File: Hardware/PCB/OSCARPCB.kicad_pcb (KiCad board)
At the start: 2 copper layers, 1 part

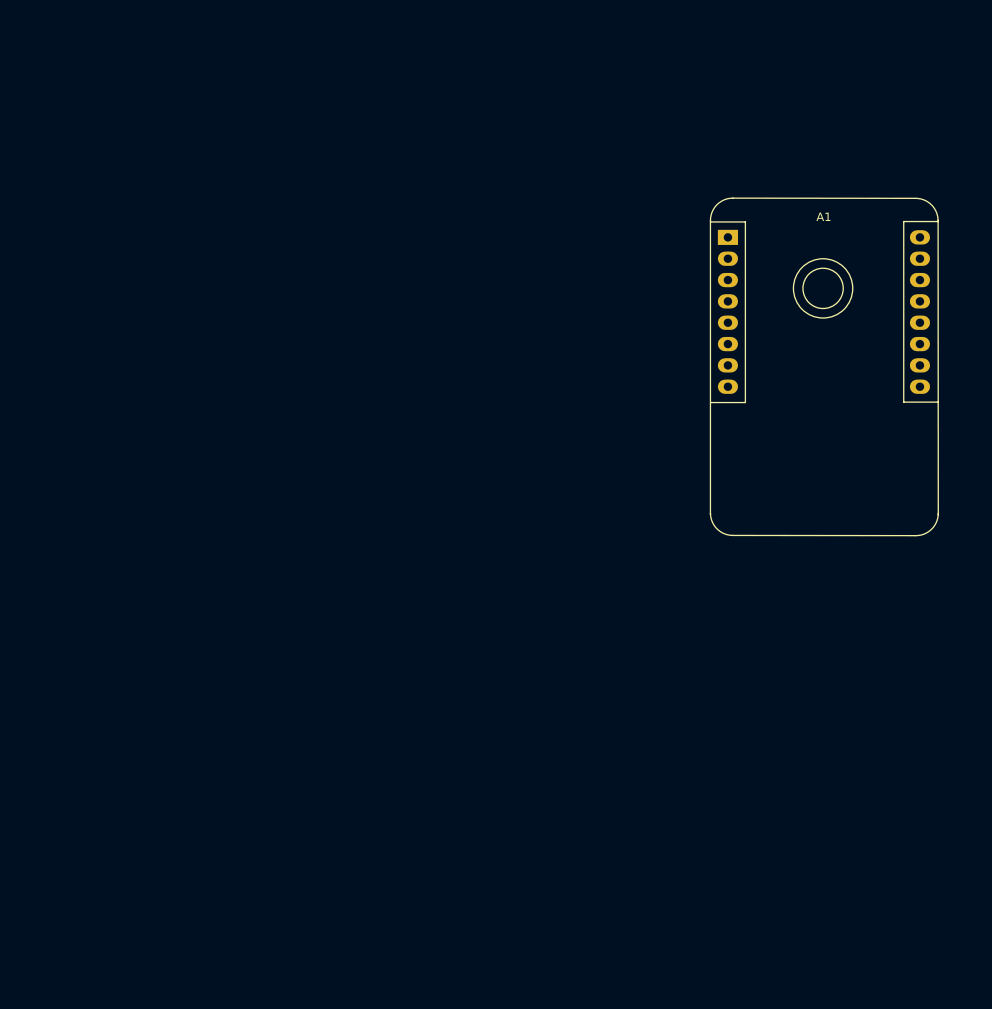
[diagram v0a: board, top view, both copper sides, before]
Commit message: Started routing PCB
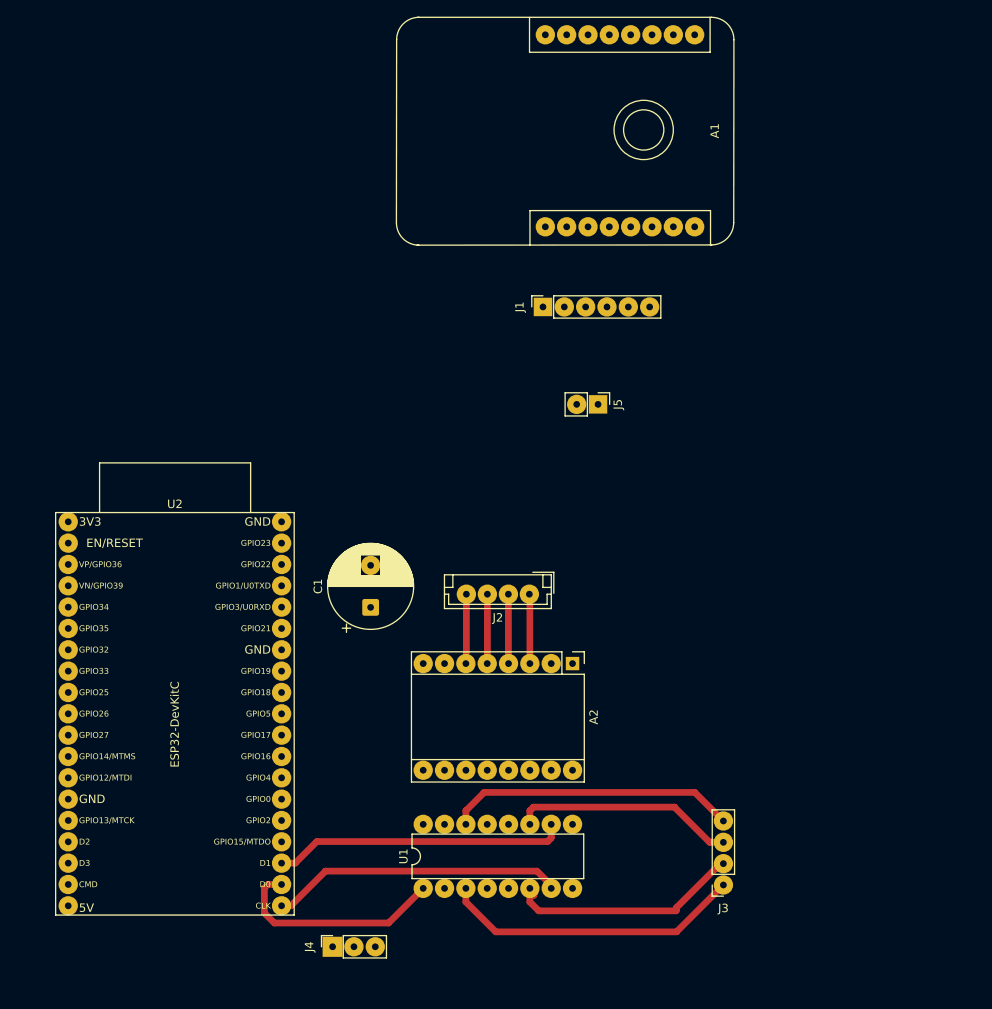
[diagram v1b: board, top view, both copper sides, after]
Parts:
- added A2: Pololu_Breakout_DRV8825, Module:Pololu_Breakout-16_15.2x20.3mm, F.Cu at (95.6, 106.5)
- added C1: 220uF_50V, Capacitor_THT:CP_Radial_D10.0mm_P5.00mm, F.Cu at (71.6, 99.8)
- added J1: CP2102 IN, Connector_PinSocket_2.54mm:PinSocket_1x06_P2.54mm_Vertical, F.Cu at (92.1, 64.0)
- added J2: Stepper Motor OUT, Connector_JST:JST_EH_B4B-EH-A_1x04_P2.50mm_Vertical, F.Cu at (90.5, 98.2)
- added J3: DC Motors OUT, Connector_PinSocket_2.54mm:PinSocket_1x04_P2.54mm_Vertical, F.Cu at (113.6, 132.8)
- added J4: Servo OUT, Connector_PinSocket_2.54mm:PinSocket_1x03_P2.54mm_Vertical, F.Cu at (67.1, 140.2)
- added J5: Power Input, Connector_PinHeader_2.54mm:PinHeader_1x02_P2.54mm_Vertical, F.Cu at (98.7, 75.6)
- added U1: L293D, Package_DIP:DIP-16_W7.62mm, F.Cu at (77.9, 133.2)
- added U2: ESP32-DevKitC, PCM_Espressif:ESP32-DevKitC, F.Cu at (35.6, 89.6)
- moved A1 36.7 mm to (98.3, 42.9), turned to -90 degrees
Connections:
- A1 pad 10: unconnected-(A1-TX-Pad10) -> Net-(A1-TX)
- A1 pad 11: unconnected-(A1-RX-Pad11) -> Net-(A1-RX)
- A1 pad 12: unconnected-(A1-VCC-Pad12) -> VBATT
- A1 pad 13: unconnected-(A1-GND-Pad13) -> GND
- A1 pad 2: unconnected-(A1-GND-Pad2) -> GND
- A1 pad 9: unconnected-(A1-GND-Pad9) -> GND
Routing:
- net /L Motor +: track 0.00 -> 36.1 mm
- net /R Motor 3: track 0.00 -> 35.0 mm
- net /L Motor 2: track 0.00 -> 34.9 mm
- net /R Motor -: track 0.00 -> 34.6 mm
- net /L Motor -: track 0.00 -> 30.5 mm
- net /R Motor +: track 0.00 -> 26.6 mm
- net /L Motor EN: track 0.00 -> 26.3 mm
- net /S. B2: track 0.00 -> 8.28 mm
- net /S. A2: track 0.00 -> 8.28 mm
- net /S. B1: track 0.00 -> 8.27 mm
- net /S. A1: track 0.00 -> 8.27 mm

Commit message: changed sch to fit PCB better
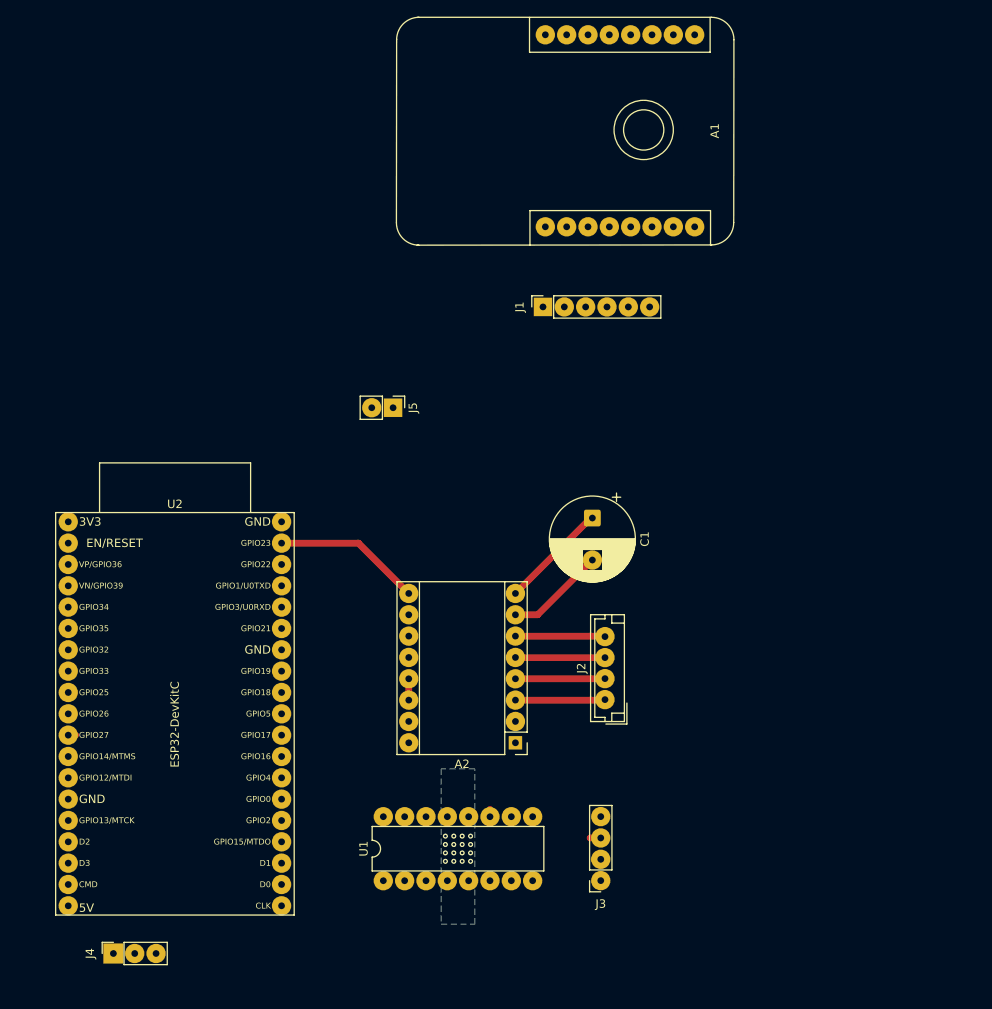
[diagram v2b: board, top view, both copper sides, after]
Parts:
- moved C1 28.5 mm to (98.0, 89.1), turned to -90 degrees
- moved J4 26.1 mm to (41.0, 141.0)
- moved J5 24.4 mm to (74.3, 76.0)
- moved J2 15.4 mm to (99.5, 110.8), turned to 90 degrees
- moved J3 14.6 mm to (99.0, 132.3)
- moved A2 11.6 mm to (88.8, 115.9), turned to 180 degrees
- moved U1 4.84 mm to (73.1, 132.3)
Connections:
- A2 pad 10: /S. M0 -> unconnected-(A2-M0-Pad10)
- A2 pad 9: /S. EN -> EN
- U2 pad 37: /S. M0 -> EN
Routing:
- net /L Motor +: track 36.1 -> 0.00 mm
- net /R Motor 3: track 35.0 -> 0.00 mm
- net /L Motor 2: track 34.9 -> 0.00 mm
- net /R Motor -: track 34.6 -> 0.00 mm
- net /L Motor -: track 30.5 -> 0.81 mm
- net /L Motor EN: track 26.3 -> 0.63 mm
- net /R Motor +: track 26.6 -> 2.16 mm
- net EN: track 0.00 -> 17.6 mm
- net VMOT: track 0.00 -> 12.9 mm
- net GND: track 0.00 -> 11.9 mm, vias 0 -> 16
- net /S. SLP + RST: track 0.00 -> 2.54 mm
- net /S. B1: track 8.27 -> 10.7 mm
- net /S. A2: track 8.28 -> 10.7 mm
- net /S. A1: track 8.27 -> 10.7 mm
- net /S. B2: track 8.28 -> 10.7 mm
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- added copper zone on B.Cu, net GND

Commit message: PCB V1
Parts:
- removed A1: ESP32_CAM, PCM_SL_Development_Boards:ESP32-CAM
- removed J1: CP2102 IN, Connector_PinSocket_2.54mm:PinSocket_1x06_P2.54mm_Vertical
- added CAM Power: PINHD_1x2_Female, Connector_PinSocket_2.54mm:PinSocket_1x02_P2.54mm_Vertical, F.Cu at (72.5, 78.5)
- DC Motors: renamed from J3
- Power In: renamed from J5
- Stepper Motor: renamed from J2
- moved Servo 23.4 mm to (64.4, 141.0)
- moved Power In 9.87 mm to (70.2, 85.0), turned to 90 degrees
- renumbered J4 to Servo
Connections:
- net /L Motor 2 renamed Net-(U1-2A)
- net /S. SLP + RST renamed SLP / RST
- A2 pad 10: unconnected-(A2-M0-Pad10) -> M0
- A2 pad 11: /S. M1 -> M1
- A2 pad 12: /S. M2 -> M2
- A2 pad 15: /S. STEP -> STEP
- A2 pad 16: /S. DIR -> DIR
- A2 pad 2: /S. FLT -> FLT
- A2 pad 7: GND -> GND VMOT
- C1 pad 2: GND -> GND VMOT
- Servo pad 1: /Servo PWM -> Net-(U2-MTCK/GPIO13/ADC2_CH4)
- U1 pad 1: /L Motor EN -> Net-(U1-EN1,2)
- U1 pad 10: /R Motor 3 -> R Motor 3
- U1 pad 15: /R Motor 4 -> R Motor 4
- U1 pad 2: /L Motor 1 -> Net-(U1-1A)
- U1 pad 9: /R Motor EN -> R EN
- U2 pad 10: /S. M2 -> unconnected-(U2-DAC_2/ADC2_CH9/GPIO26-Pad10)
- U2 pad 11: /L Motor 1 -> unconnected-(U2-ADC2_CH7/GPIO27-Pad11)
- U2 pad 15: unconnected-(U2-MTCK/GPIO13/ADC2_CH4-Pad15) -> Net-(U2-MTCK/GPIO13/ADC2_CH4)
- U2 pad 16: NC -> unconnected-(U2-SD_DATA2/GPIO9-Pad16)
- U2 pad 17: NC -> unconnected-(U2-SD_DATA3/GPIO10-Pad17)
- U2 pad 18: NC -> unconnected-(U2-CMD-Pad18)
- U2 pad 21: /L Motor EN -> Net-(U1-1A)
- U2 pad 22: /R Motor 3 -> Net-(U1-EN1,2)
- U2 pad 23: /Servo PWM -> unconnected-(U2-MTDO/GPIO15/ADC2_CH3-Pad23)
- U2 pad 24: unconnected-(U2-ADC2_CH2/GPIO2-Pad24) -> R Motor 4
- U2 pad 26: unconnected-(U2-ADC2_CH0/GPIO4-Pad26) -> R Motor 3
- U2 pad 27: /R Motor 4 -> R EN
- U2 pad 28: /R Motor EN -> DIR
- U2 pad 29: /S. FLT -> STEP
- U2 pad 31: /S. EN -> M2
- U2 pad 33: /S. STEP -> M1
- U2 pad 36: /S. DIR -> M0
- U2 pad 9: /S. M1 -> unconnected-(U2-DAC_1/ADC2_CH8/GPIO25-Pad9)
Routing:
- net GND: track 11.9 -> 175.7 mm, vias 16 -> 0
- net VBATT: track 0.00 -> 136.8 mm
- net Net-(U2-MTCK/GPIO13/ADC2_CH4): track 0.00 -> 35.4 mm
- net R EN: track 0.00 -> 33.8 mm
- net R Motor 3: track 0.00 -> 30.2 mm
- net /L Motor +: track 0.00 -> 29.8 mm
- net Net-(U1-2A): track 0.00 -> 29.8 mm
- net /R Motor -: track 0.00 -> 29.5 mm
- net SLP / RST: track 2.54 -> 20.4 mm
- net M0: track 0.00 -> 17.6 mm
- net Net-(U1-1A): track 0.00 -> 17.1 mm
- net R Motor 4: track 0.00 -> 16.9 mm
- net M2: track 0.00 -> 15.8 mm
- net STEP: track 0.00 -> 15.5 mm
- net DIR: track 0.00 -> 15.5 mm
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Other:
- board outline added: 77.5 x 73 mm

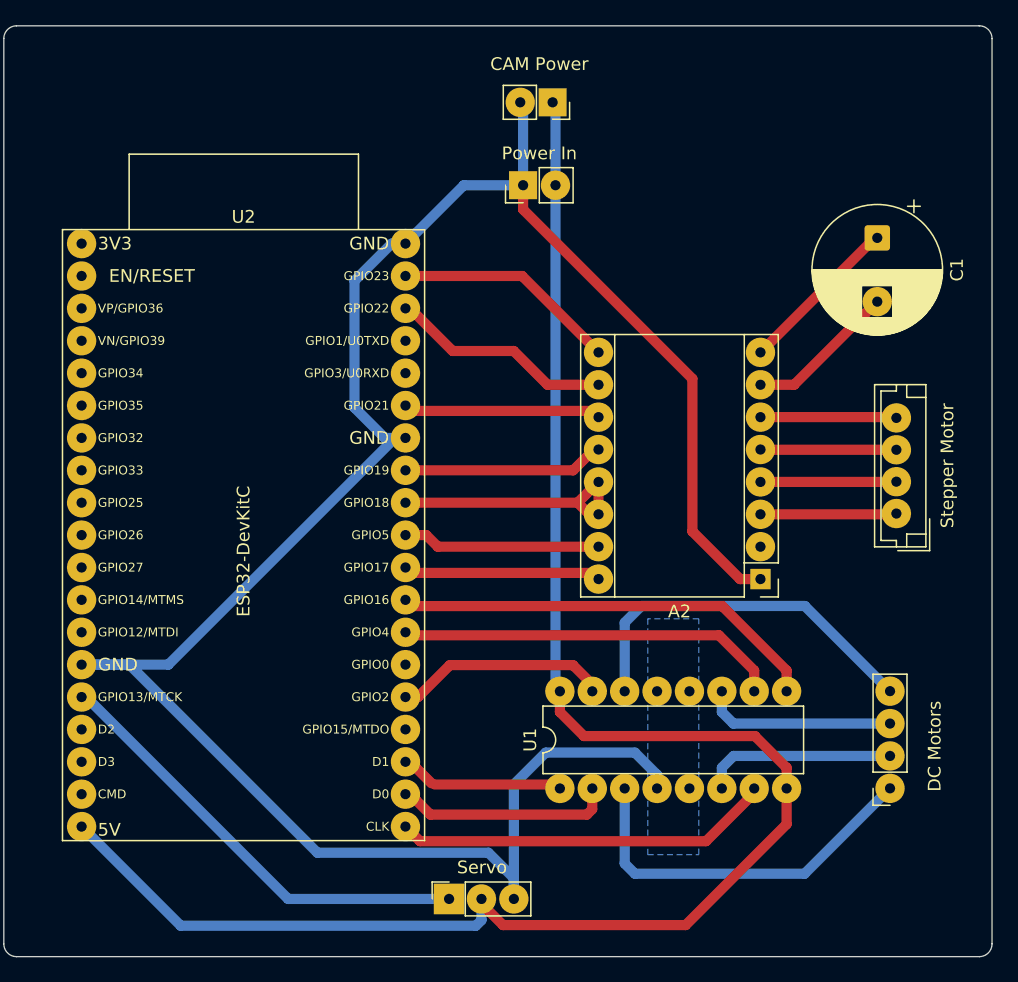
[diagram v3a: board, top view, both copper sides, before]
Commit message: Updated PCB becasue Im using external components
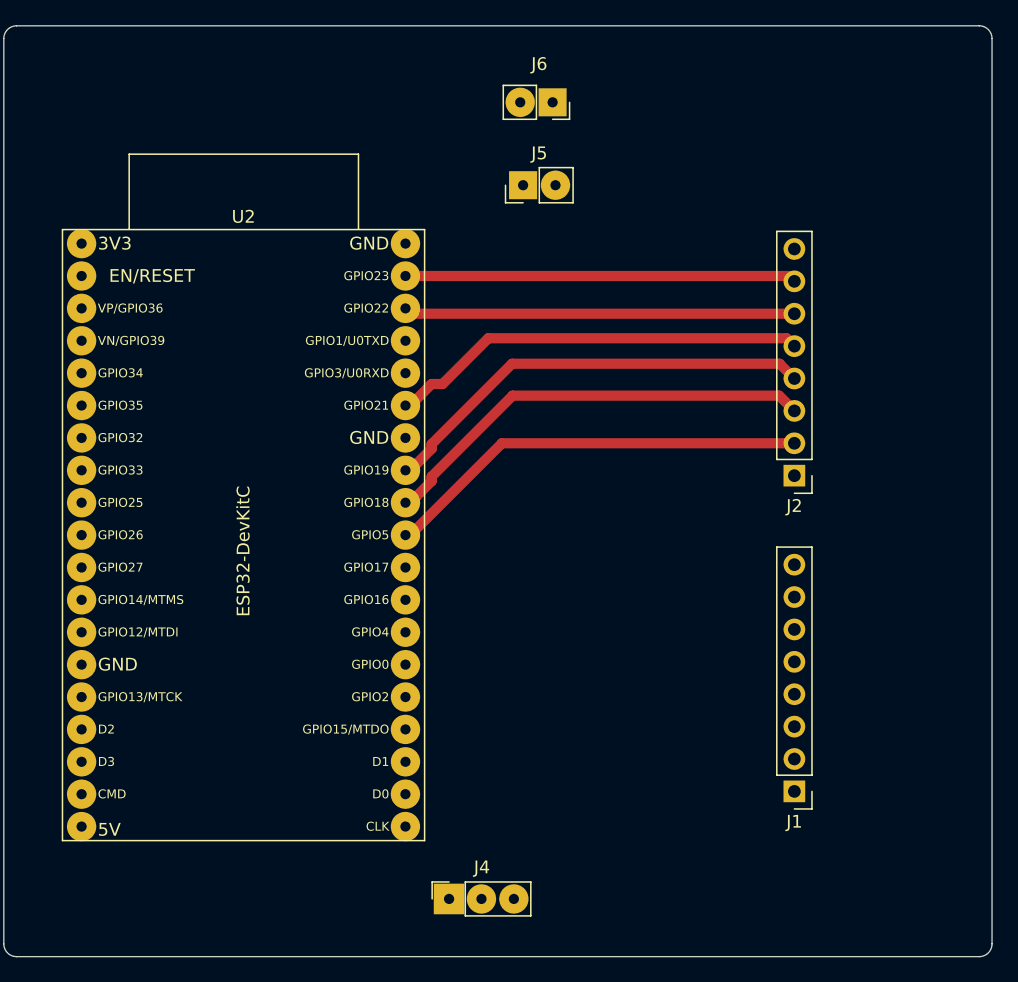
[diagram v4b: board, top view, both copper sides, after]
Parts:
- removed A2: Pololu_Breakout_DRV8825, Module:Pololu_Breakout-16_15.2x20.3mm
- removed C1: 220uF_50V, Capacitor_THT:CP_Radial_D10.0mm_P5.00mm
- removed DC Motors: DC Motors OUT, Connector_PinSocket_2.54mm:PinSocket_1x04_P2.54mm_Vertical
- removed Stepper Motor: Stepper Motor OUT, Connector_JST:JST_EH_B4B-EH-A_1x04_P2.50mm_Vertical
- removed U1: L293D, Package_DIP:DIP-16_W7.62mm
- added J1: PINHD_1x8_Male, Connector_PinHeader_2.54mm:PinHeader_1x08_P2.54mm_Vertical, F.Cu at (91.5, 132.5)
- added J2: PINHD_1x8_Male, Connector_PinHeader_2.54mm:PinHeader_1x08_P2.54mm_Vertical, F.Cu at (91.5, 107.8)
- J5: renamed from Power In
- J6: renamed from CAM Power
- renumbered Servo to J4
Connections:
- U2 pad 29: STEP -> Net-(U2-GPIO5)
- U2 pad 30: SLP / RST -> Net-(U2-GPIO18)
- U2 pad 31: M2 -> Net-(U2-GPIO19)
- U2 pad 33: M1 -> Net-(U2-GPIO21)
- U2 pad 36: M0 -> Net-(U2-GPIO22)
- U2 pad 37: EN -> Net-(U2-GPIO23)
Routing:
- net GND: track 175.7 -> 0.00 mm
- net VBATT: track 136.8 -> 0.00 mm
- net Net-(U2-MTCK/GPIO13/ADC2_CH4): track 35.4 -> 0.00 mm
- net Net-(U2-GPIO18): track 0.00 -> 34.7 mm
- net Net-(U2-GPIO19): track 0.00 -> 34.7 mm
- net R EN: track 33.8 -> 0.00 mm
- net Net-(U2-GPIO5): track 0.00 -> 33.5 mm
- net Net-(U2-GPIO21): track 0.00 -> 32.9 mm
- net Net-(U2-GPIO23): track 0.00 -> 30.7 mm
- net Net-(U2-GPIO22): track 0.00 -> 30.7 mm
- net R Motor 3: track 30.2 -> 0.00 mm
- net /L Motor +: track 29.8 -> 0.00 mm
- net Net-(U2-SD_CLK/GPIO6): track 29.8 -> 0.00 mm
- net /R Motor -: track 29.5 -> 0.00 mm
- net SLP / RST: track 20.4 -> 0.00 mm
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- removed copper zone on B.Cu, net GND

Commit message: PCB Done?
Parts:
- J1: value PINHD_1x8_Male -> DC Motor; footprint Connector_PinHeader_2.54mm:PinHeader_1x08_P2.54mm_Vertical -> Connector_PinHeader_2.54mm:PinHeader_1x06_P2.54mm_Vertical
- J2: value PINHD_1x8_Male -> Stepper Motor; footprint Connector_PinHeader_2.54mm:PinHeader_1x08_P2.54mm_Vertical -> Connector_PinHeader_2.54mm:PinHeader_1x06_P2.54mm_Vertical
- moved J6 85.5 mm to (136.0, 135.8), turned to 0 degrees
- moved U2 67.6 mm to (103.1, 85.6)
- moved J5 65.9 mm to (109.0, 138.3), turned to 180 degrees
- moved J2 48.0 mm to (139.5, 108.6)
- moved J1 36.9 mm to (96.0, 95.9), turned to 0 degrees
- moved J4 36.0 mm to (95.0, 122.0), turned to 180 degrees
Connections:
- J1 pad 1: VBATT -> L Motor EN
- J1 pad 2: Net-(U2-SD_CLK/GPIO6) -> L Motor 1
- J1 pad 3: Net-(U2-SD_DATA0/GPIO7) -> L Motor 2
- J1 pad 4: Net-(U2-SD_DATA1/GPIO8) -> R Motor 3
- J1 pad 5: R Motor 3 -> R Motor 4
- J1 pad 6: R Motor 4 -> R EN
- J2 pad 1: unconnected-(J2-Pad1) -> Net-(U2-GPIO5)
- J2 pad 2: Net-(U2-GPIO5) -> Net-(U2-GPIO18)
- J2 pad 3: Net-(U2-GPIO18) -> Net-(U2-GPIO19)
- J2 pad 4: Net-(U2-GPIO19) -> Net-(U2-GPIO21)
- J2 pad 5: Net-(U2-GPIO21) -> Net-(U2-GPIO22)
- J2 pad 6: Net-(U2-GPIO22) -> Net-(U2-GPIO23)
- U2 pad 10: unconnected-(U2-DAC_2/ADC2_CH9/GPIO26-Pad10) -> R EN
- U2 pad 20: Net-(U2-SD_CLK/GPIO6) -> unconnected-(U2-SD_CLK/GPIO6-Pad20)
- U2 pad 21: Net-(U2-SD_DATA0/GPIO7) -> unconnected-(U2-SD_DATA0/GPIO7-Pad21)
- U2 pad 22: Net-(U2-SD_DATA1/GPIO8) -> unconnected-(U2-SD_DATA1/GPIO8-Pad22)
- U2 pad 24: R Motor 4 -> unconnected-(U2-ADC2_CH2/GPIO2-Pad24)
- U2 pad 26: R Motor 3 -> unconnected-(U2-ADC2_CH0/GPIO4-Pad26)
- U2 pad 27: R EN -> unconnected-(U2-GPIO16-Pad27)
- U2 pad 28: DIR -> unconnected-(U2-GPIO17-Pad28)
- U2 pad 5: unconnected-(U2-VDET_1/GPIO34/ADC1_CH6-Pad5) -> L Motor EN
- U2 pad 6: unconnected-(U2-VDET_2/GPIO35/ADC1_CH7-Pad6) -> L Motor 1
- U2 pad 7: unconnected-(U2-32K_XP/GPIO32/ADC1_CH4-Pad7) -> L Motor 2
- U2 pad 8: unconnected-(U2-32K_XN/GPIO33/ADC1_CH5-Pad8) -> R Motor 3
- U2 pad 9: unconnected-(U2-DAC_1/ADC2_CH8/GPIO25-Pad9) -> R Motor 4
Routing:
- net GND: track 0.00 -> 120.9 mm
- net VBATT: track 0.00 -> 60.2 mm
- net Net-(U2-GPIO18): track 34.7 -> 12.1 mm
- net Net-(U2-GPIO19): track 34.7 -> 12.1 mm
- net Net-(U2-GPIO5): track 33.5 -> 11.1 mm
- net Net-(U2-GPIO21): track 32.9 -> 12.8 mm
- net Net-(U2-GPIO23): track 30.7 -> 14.2 mm
- net Net-(U2-GPIO22): track 30.7 -> 14.8 mm
- net Net-(U2-MTCK/GPIO13/ADC2_CH4): track 0.00 -> 8.56 mm
- net R Motor 4: track 0.00 -> 7.49 mm
- net L Motor 2: track 0.00 -> 7.49 mm
- net R Motor 3: track 0.00 -> 7.49 mm
- net R EN: track 0.00 -> 7.49 mm
- net L Motor EN: track 0.00 -> 7.49 mm
- net L Motor 1: track 0.00 -> 7.49 mm
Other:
- board size 77.5 x 73 mm -> 59.5 x 68 mm
